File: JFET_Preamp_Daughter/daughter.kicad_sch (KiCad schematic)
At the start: 19 parts, among them J101 Conn_01x08_Socket, J102 Conn_01x06_Socket, J103 Conn_01x06_Socket, U101 PCM1865DBTR

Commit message: finish draft of mother/daughter sch and start routing, reconcile libraries and missing footprints
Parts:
- added R102, R103: 0, symbol Device:R
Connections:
- net GND: now also R102.1, R102.2
- net MCLK: now also R103.1; no longer J101.3 (Pin_3)
- new net: J101.3 (Pin_3), R103.2

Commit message: adding a few minor edits
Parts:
- removed J102, J103: Conn_01x06_Socket, symbol Connector:Conn_01x06_Socket
- added J102, J103: Conn_01x06, Connector_PinHeader_2.54mm:PinHeader_1x06_P2.54mm_Vertical, symbol Connector_Generic:Conn_01x06
- C101, C102, C103, C104, C105, C106, C107, C108, C109, C110, C111, C112, C113: footprint (none) -> Capacitor_SMD:C_0201_0603Metric
- D101: footprint (none) -> LED_SMD:LED_0603_1608Metric
- J101: footprint (none) -> Connector_JST:JST_GH_BM08B-GHS-TBT_1x08-1MP_P1.25mm_Vertical
- R101, R102, R103: footprint (none) -> Resistor_SMD:R_0603_1608Metric
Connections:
- net CH1_COLD: now also J103.1 (Pin_1)
- net CH1_HOT: now also J103.5 (Pin_5)
- net CH2_COLD: now also J103.2 (Pin_2)
- net CH2_HOT: now also J103.6 (Pin_6)
- net CH3_COLD: now also J102.1 (Pin_1)
- net CH3_HOT: now also J102.5 (Pin_5)
- net CH4_COLD: now also J102.2 (Pin_2)
- net CH4_HOT: now also J102.6 (Pin_6)
- net GND: now also J102.3 (Pin_3), J102.4 (Pin_4), J103.3 (Pin_3), J103.4 (Pin_4)
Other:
- moved on the sheet: J101, R103

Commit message: finish routing daughterboard and fix 0 ohm resistor on AGND/DGND for schematic
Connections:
- net GND: no longer R102.1, U101.7 (AGND)
- new net: R102.1, U101.7 (AGND)
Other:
- moved on the sheet: R102
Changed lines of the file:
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@@
 	)
 	(junction
-		(at 80.01 100.33)
+		(at 86.36 99.06)
 		(diameter 0)
 		(color 0 0 0 0)
@@
 	)
 	(junction
-		(at 71.12 96.52)
+		(at 77.47 97.79)
 		(diameter 0)
 		(color 0 0 0 0)
@@
 	)
 	(junction
-		(at 69.85 106.68)
-		(diameter 0)
-		(color 0 0 0 0)
-	)
-	(junction
 		(at 167.64 39.37)
 		(diameter 0)
@@
 	(wire
 		(pts
+			(xy 77.47 96.52) (xy 77.47 97.79)
+		)
+		(stroke
+			(width 0)
+			(type default)
+		)
+	)
+	(wire
+		(pts
 			(xy 76.2 20.32) (xy 83.82 20.32)
 		)
@@
 	(wire
 		(pts
-			(xy 69.85 96.52) (xy 71.12 96.52)
-		)
-		(stroke
-			(width 0)
-			(type default)
-		)
-	)
-	(wire
-		(pts
 			(xy 115.57 73.66) (xy 104.14 73.66)
 		)
@@
 	(wire
 		(pts
+			(xy 77.47 97.79) (xy 77.47 99.06)
+		)
+		(stroke
+			(width 0)
+			(type default)
+		)
+	)
+	(wire
+		(pts
 			(xy 160.02 16.51) (xy 168.91 16.51)
 		)
@@
 	(wire
 		(pts
-			(xy 80.01 100.33) (xy 80.01 106.68)
+			(xy 86.36 99.06) (xy 86.36 106.68)
 		)
 		(stroke
@@
 	(wire
 		(pts
+			(xy 77.47 96.52) (xy 86.36 96.52)
+		)
+		(stroke
+			(width 0)
+			(type default)
+		)
+	)
+	(wire
+		(pts
 			(xy 62.23 30.48) (xy 62.23 27.94)
 		)
@@
 	(wire
 		(pts
-			(xy 86.36 96.52) (xy 71.12 96.52)
-		)
-		(stroke
-			(width 0)
-			(type default)
-		)
-	)
-	(wire
-		(pts
 			(xy 43.18 53.34) (xy 43.18 57.15)
 		)
@@
 	(wire
 		(pts
-			(xy 80.01 100.33) (xy 78.74 100.33)
+			(xy 86.36 99.06) (xy 85.09 99.06)
 		)
 		(stroke
@@
 	(wire
 		(pts
-			(xy 71.12 96.52) (xy 71.12 100.33)
-		)
-		(stroke
-			(width 0)
-			(type default)
-		)
-	)
-	(wire
-		(pts
 			(xy 167.64 39.37) (xy 167.64 53.34)
 		)
@@
 	(wire
 		(pts
-			(xy 69.85 106.68) (xy 69.85 96.52)
-		)
-		(stroke
-			(width 0)
-			(type default)
-		)
-	)
-	(wire
-		(pts
 			(xy 54.61 105.41) (xy 62.23 105.41)
 		)
@@
 	(wire
 		(pts
-			(xy 91.44 96.52) (xy 91.44 100.33)
+			(xy 91.44 96.52) (xy 91.44 99.06)
 		)
 		(stroke
@@
 	(wire
 		(pts
-			(xy 91.44 100.33) (xy 80.01 100.33)
+			(xy 91.44 99.06) (xy 86.36 99.06)
 		)
 		(stroke
@@
 	(wire
 		(pts
-			(xy 69.85 106.68) (xy 80.01 106.68)
+			(xy 62.23 106.68) (xy 86.36 106.68)
 		)
 		(stroke
@@
 		(pts
 			(xy 57.15 73.66) (xy 57.15 63.5)
-		)
-		(stroke
-			(width 0)
-			(type default)
-		)
-	)
-	(wire
-		(pts
-			(xy 62.23 106.68) (xy 69.85 106.68)
 		)
 		(stroke
@@
 	(symbol
 		(lib_id "Device:R")
-		(at 74.93 100.33 90)
+		(at 81.28 99.06 90)
 		(unit 1)
 		(body_style 1)
@@
 		(dnp no)
 		(property "Reference" "R102"
-			(at 74.93 102.616 90)
+			(at 81.28 101.346 90)
 			(show_name no)
 			(do_not_autoplace no)
@@
 		)
 		(property "Value" "0"
-			(at 76.708 104.648 90)
+			(at 83.058 103.378 90)
 			(show_name no)
 			(do_not_autoplace no)
@@
 		)
 		(property "Footprint" "Resistor_SMD:R_0603_1608Metric"
-			(at 74.93 102.108 90)
+			(at 81.28 100.838 90)
 			(hide yes)
 			(show_name no)
@@
 		)
 		(property "Datasheet" ""
-			(at 74.93 100.33 0)
+			(at 81.28 99.06 0)
 			(hide yes)
 			(show_name no)
@@
 		)
 		(property "Description" "Resistor"
-			(at 74.93 100.33 0)
+			(at 81.28 99.06 0)
 			(hide yes)
 			(show_name no)
@@
 					(unit 1)
 				)
+			)
+		)
+	)
+	(symbol
+		(lib_id "power:PWR_FLAG")
+		(at 77.47 97.79 90)
+		(unit 1)
+		(body_style 1)
+		(exclude_from_sim no)
+		(in_bom yes)
+		(on_board yes)
+		(in_pos_files yes)
+		(dnp no)
+		(property "Reference" "#FLG0203"
+			(at 75.565 97.79 0)
+			(hide yes)
+			(show_name no)
+			(do_not_autoplace no)
+			(effects
+				(font
+					(size 1.27 1.27)
+				)
+			)
+		)
+		(property "Value" "PWR_FLAG"
+			(at 73.914 98.552 0)
+			(show_name no)
+			(do_not_autoplace no)
+			(effects
+				(font
+					(size 1.27 1.27)
+				)
+			)
+		)
+		(property "Footprint" ""
+			(at 77.47 97.79 0)
+			(hide yes)
+			(show_name no)
+			(do_not_autoplace no)
+			(effects
+				(font
+					(size 1.27 1.27)
+				)
+			)
+		)
+		(property "Datasheet" ""
+			(at 77.47 97.79 0)
+			(hide yes)
+			(show_name no)
+			(do_not_autoplace no)
+			(effects
+				(font
+					(size 1.27 1.27)
+				)
+			)
+		)
+		(property "Description" "Special symbol for telling ERC where power comes from"
+			(at 77.47 97.79 0)
+			(hide yes)
+			(show_name no)
+			(do_not_autoplace no)
+			(effects
+				(font
+					(size 1.27 1.27)
+				)
+			)
+		)
+		(pin "1"
+		)
+		(instances
+			(project "daughter"
+				(path "/17cdfba3-e93c-4ecb-8cde-29ebdfd88a24"
+					(reference "#FLG0203")
+					(unit 1)
+				)

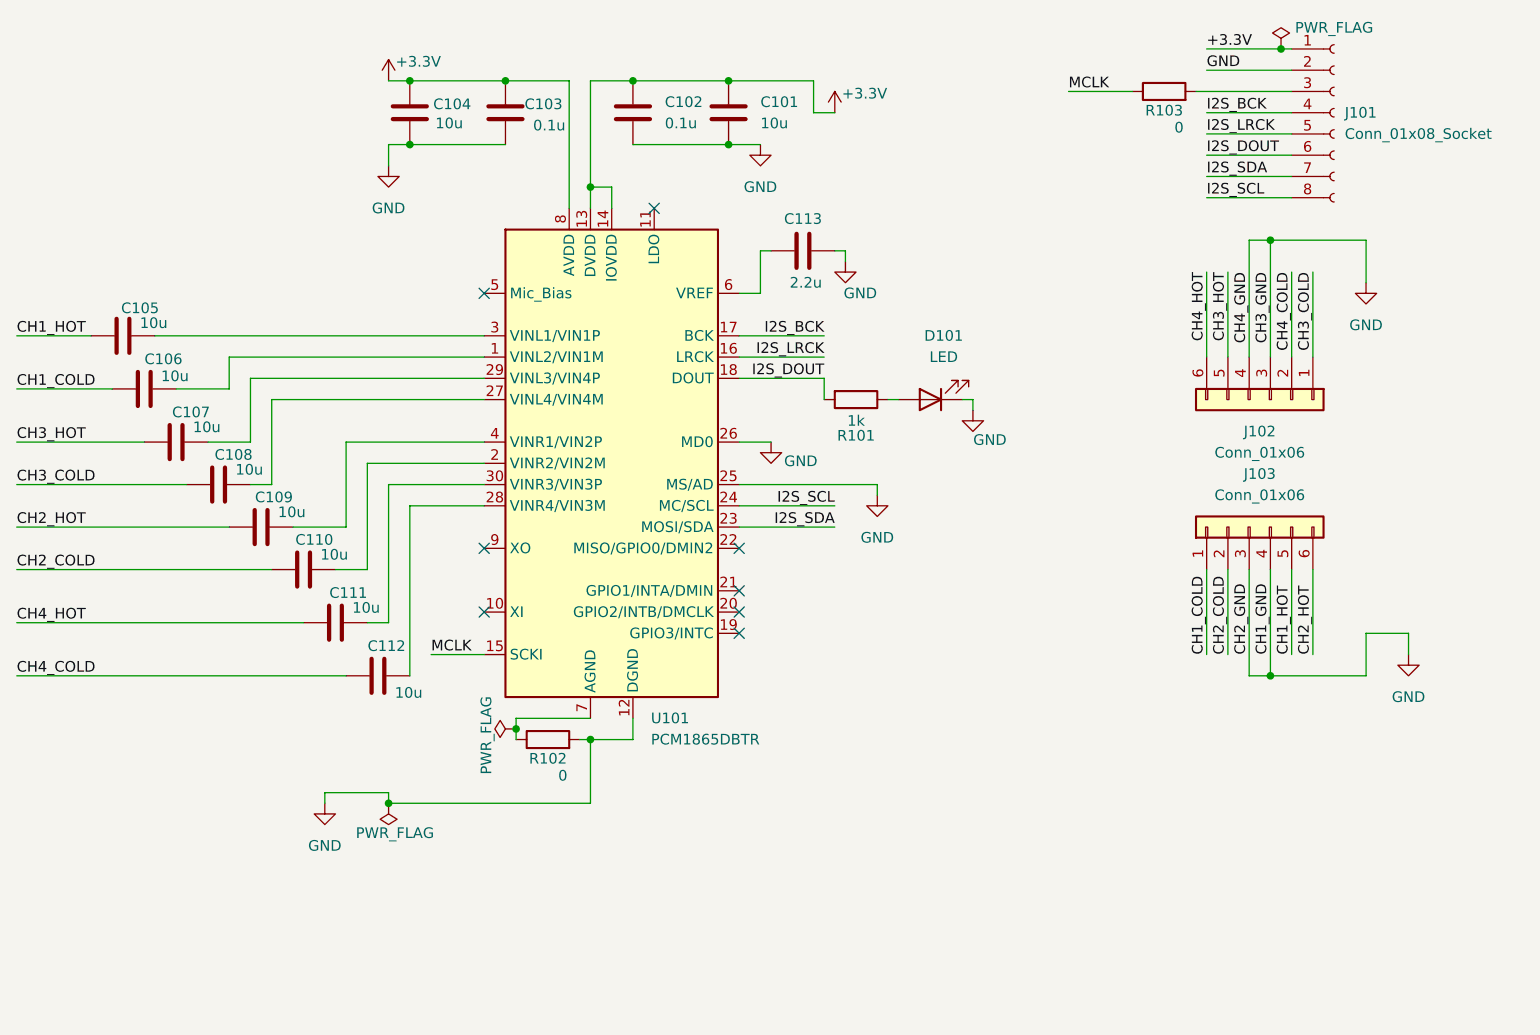
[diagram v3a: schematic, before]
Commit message: small updates to schematic before adjusting/printing pdf
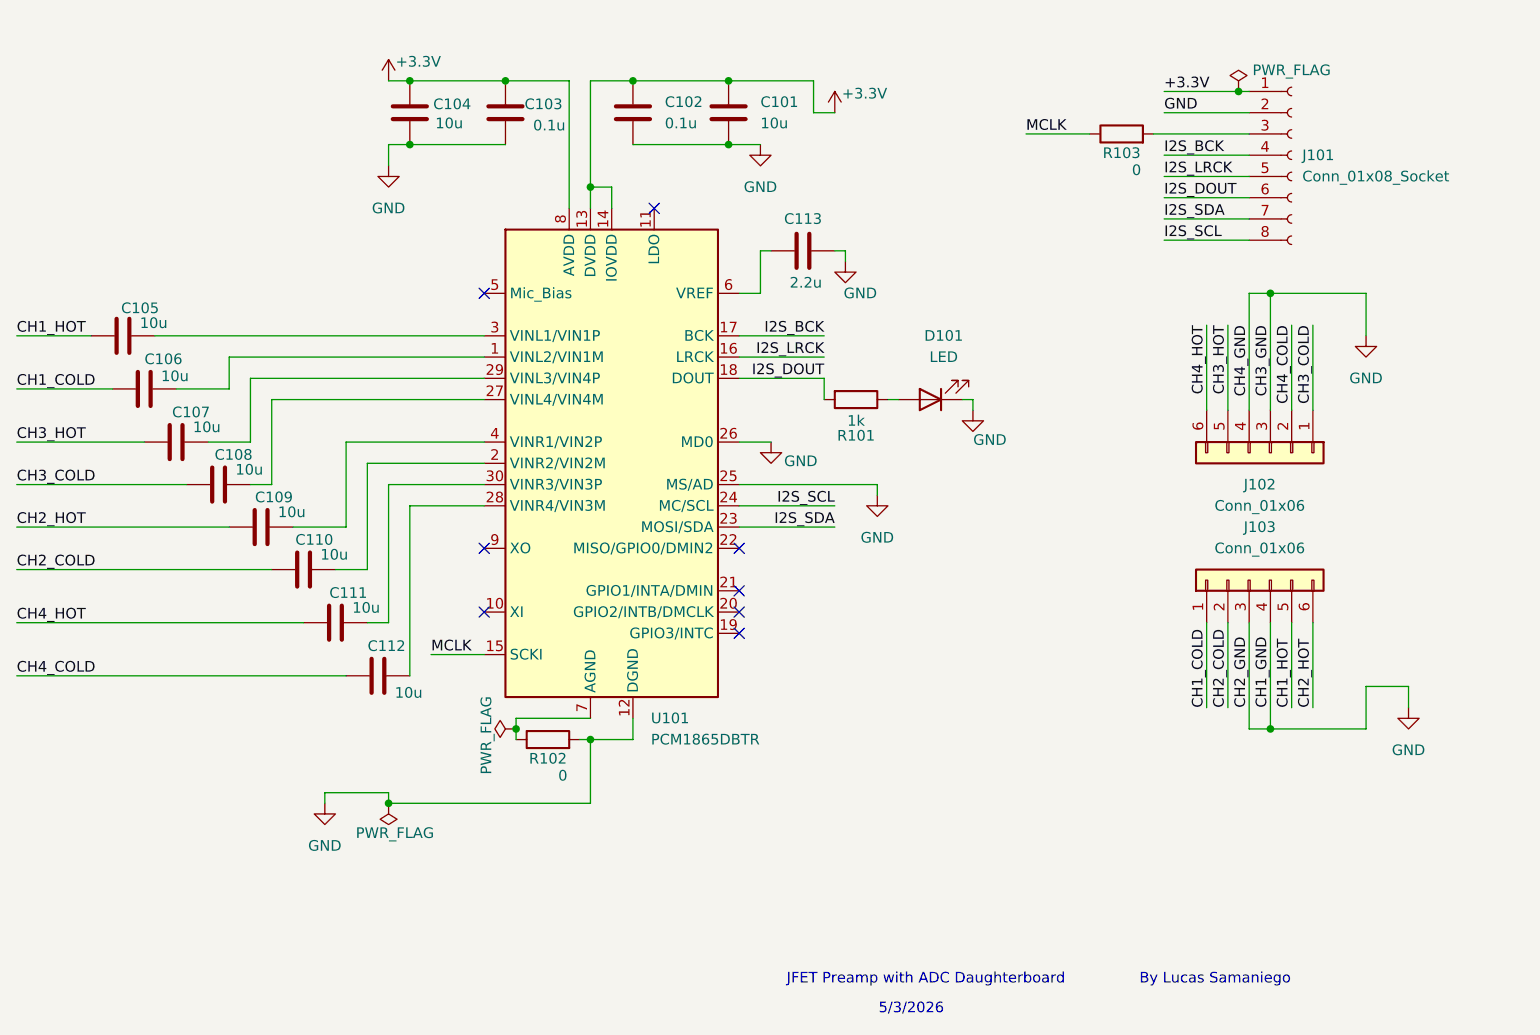
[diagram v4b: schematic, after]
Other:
- note added: "5/3/2026"
- note added: "JFET Preamp with ADC Daughterboard By Lucas Samaniego"
- moved on the sheet: J101, J102, J103, R103

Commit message: update Capacitors to better suit and rebuild, prep for fab, final for 1st fab
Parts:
- C101, C104, C105, C106, C107, C108, C109, C110, C111, C112: footprint Capacitor_SMD:C_0201_0603Metric -> Capacitor_SMD:C_0402_1005Metric; LCSC Part # (none) -> C15525
- C102, C103: footprint Capacitor_SMD:C_0201_0603Metric -> Capacitor_SMD:C_0402_1005Metric; LCSC Part # (none) -> C1525
- C113: footprint Capacitor_SMD:C_0201_0603Metric -> Capacitor_SMD:C_0402_1005Metric; LCSC Part # (none) -> C12530
- D101: LCSC Part # (none) -> C2286
- J101, J102, J103: now left out of the parts list
- R101: LCSC Part # (none) -> C21190
- R102, R103: LCSC Part # (none) -> C21189
- U101: LCSC Part # (none) -> C181312
